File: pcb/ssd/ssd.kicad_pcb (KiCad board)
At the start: 2 copper layers, 68 parts, among them J101 GCT USB4105-GF-A, J301 NTC 接口 / XH 2.50mm, J302 BTL-004A / XH 2.50mm, Q201 BSS138, Q202 BSS138, SW101 启动（BOOT）, SW102 复位（RESET）, SW301 单位切换, U101 AP63203WU-7, U102 AP63205WU-7, U201 HT16K33 / SOP28, U301 SN74LVC1G17DCKR, U401 STM32C562CET6, Y401 24MHz / CL=10pF

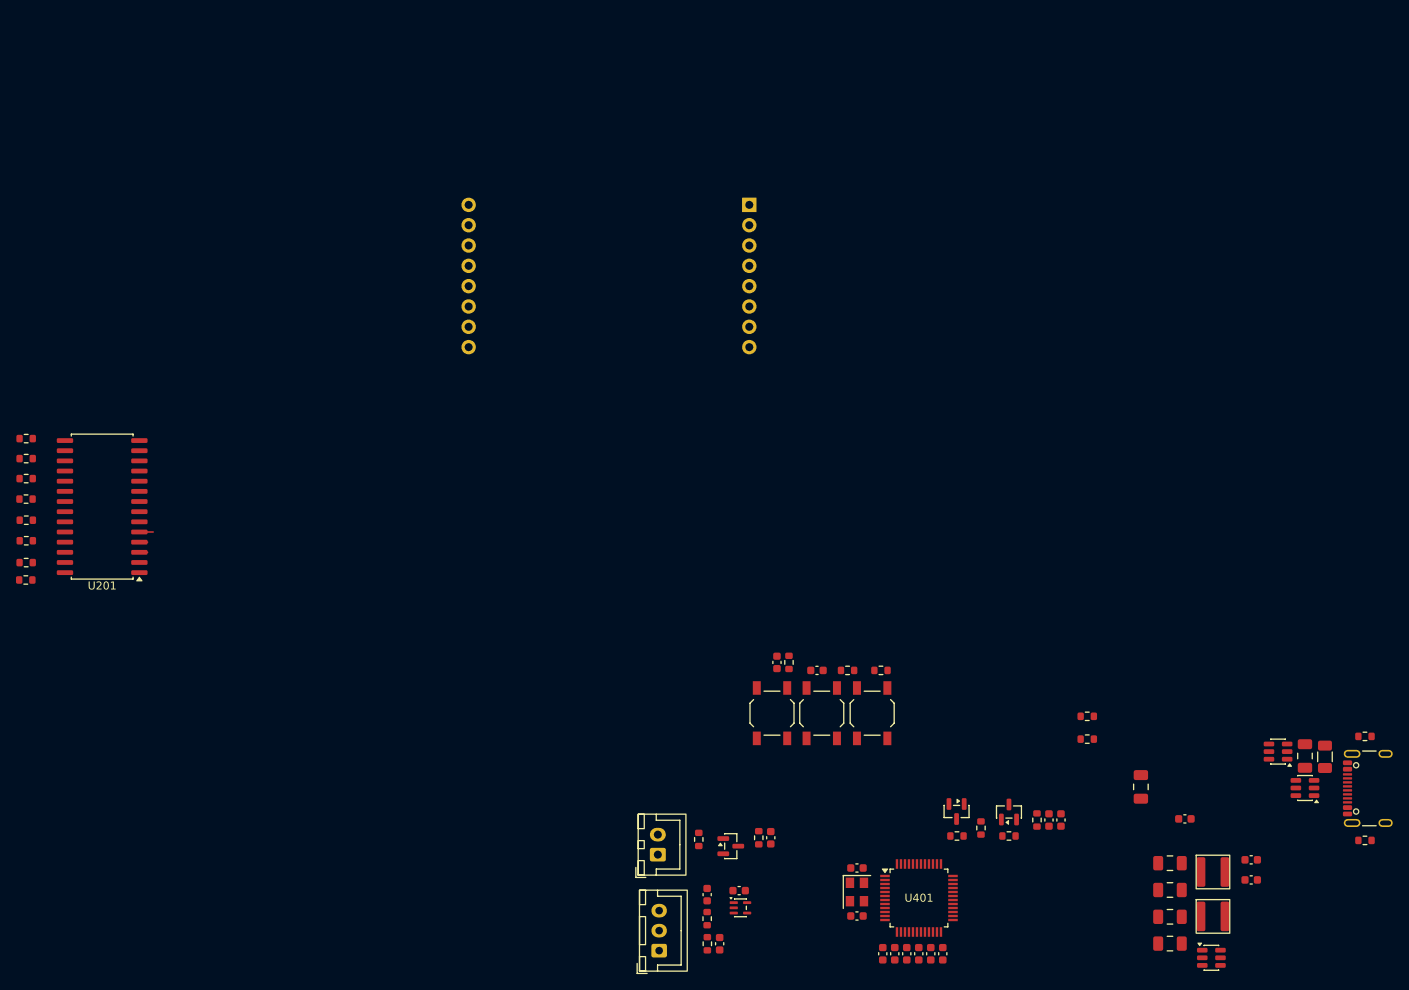
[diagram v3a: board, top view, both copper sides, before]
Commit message: 更新 Type-C 供电与 J-Link 调试设计
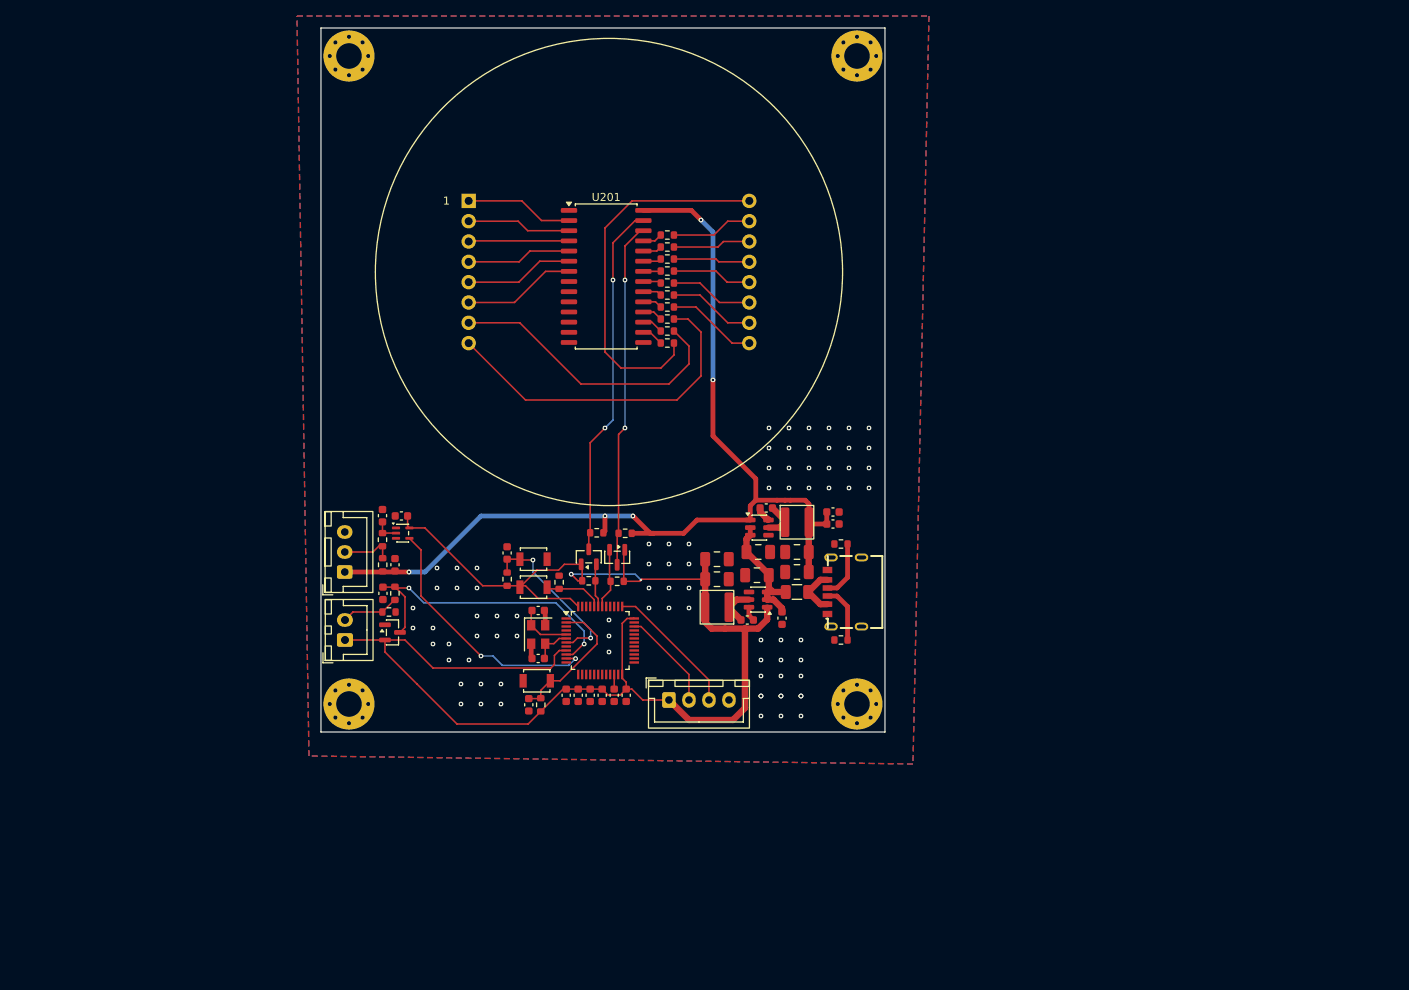
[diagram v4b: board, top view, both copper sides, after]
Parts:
- removed D101: USBLC6-2SC6, SSD:Package_TO_SOT_SMD__SOT-23-6
- added J102: SWD / XH 2.50mm, SSD:Connector_JST__JST_XH_B4B-XH-A_1x04_P2.50mm_Vertical, F.Cu at (150.0, 122.0)
- added REF**: MountingHole_3.2mm_M3_Pad_Via, MountingHole:MountingHole_3.2mm_M3_Pad_Via, F.Cu at (173.5, 122.5)
- added REF**: MountingHole_3.2mm_M3_Pad_Via, MountingHole:MountingHole_3.2mm_M3_Pad_Via, F.Cu at (110.0, 122.5)
- added REF**: MountingHole_3.2mm_M3_Pad_Via, MountingHole:MountingHole_3.2mm_M3_Pad_Via, F.Cu at (173.5, 41.5)
- added REF**: MountingHole_3.2mm_M3_Pad_Via, MountingHole:MountingHole_3.2mm_M3_Pad_Via, F.Cu at (110.0, 41.5)
- DS201: moved to F.Cu
- J101: value GCT USB4105-GF-A -> SHOU HAN TYPE-C 6P(073); footprint SSD:Connector_USB__USB_C_Receptacle_GCT_USB4105-xx-A_16P_TopMnt_Horizontal -> SSD:Connector_USB__SHOU_HAN_TYPE-C-6P-073_C668623
- SW101, SW102, SW301: footprint SSD:Button_Switch_SMD__SW_SPST_TL3342 -> SSD:Button_Switch_SMD__SW_SPST_B3U-1000P
- moved R207 87.2 mm to (149.8, 72.9), turned to 0 degrees
- moved R206 86.8 mm to (149.8, 71.4), turned to 0 degrees
- moved R205 86.4 mm to (149.8, 69.9), turned to 0 degrees
- moved R204 86.0 mm to (149.8, 68.4), turned to 0 degrees
- moved R203 85.6 mm to (149.8, 66.9), turned to 0 degrees
- moved R202 85.2 mm to (149.8, 65.4), turned to 0 degrees
- moved R201 84.9 mm to (149.8, 63.9), turned to 0 degrees
- moved R210 81.0 mm to (149.8, 77.4), turned to 0 degrees
- moved U102 78.0 mm to (161.3, 100.5)
- moved C109 76.4 mm to (162.2, 98.0)
- moved R209 73.2 mm to (149.8, 75.9)
- moved R208 72.3 mm to (149.8, 74.4), turned to 0 degrees
- moved C102 72.1 mm to (161.0, 106.4), turned to 180 degrees
- moved L102 71.6 mm to (166.0, 99.8)
- moved C110 71.0 mm to (161.2, 103.5)
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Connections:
- U401 pad 32: USB_DM -> unconnected-(U401-PA11-Pad32)
- U401 pad 33: USB_DP -> unconnected-(U401-PA12-Pad33)
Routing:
- net +3V3: track 0.00 -> 186.4 mm, vias 0 -> 2
- net +5V: track 0.00 -> 127.5 mm, vias 0 -> 5
- net Net-(DS201-J): track 0.00 -> 46.6 mm
- net Net-(Q202-D): track 0.00 -> 44.5 mm, vias 0 -> 2
- net Net-(Q201-D): track 0.00 -> 43.3 mm, vias 0 -> 2
- net Net-(DS201-H): track 0.00 -> 42.8 mm
- net NTC_ADC: track 0.00 -> 38.4 mm, vias 0 -> 2
- net Net-(DS201-I): track 0.00 -> 36.6 mm
- net FLOW_PULSE: track 0.00 -> 32.3 mm, vias 0 -> 2
- net MCU_NRST: track 0.00 -> 21.0 mm, vias 0 -> 2
- net USER_KEY: track 0.00 -> 17.5 mm
- net SWCLK: track 0.00 -> 17.2 mm
- net VIN_SYS: track 0.00 -> 15.7 mm
- net Net-(DS201-COM6): track 0.00 -> 14.2 mm
- net Net-(DS201-COM5): track 0.00 -> 13.6 mm
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- added copper zone on B.Cu, net GND
- added copper zone on F.Cu, net GND
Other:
- board outline added: 70.5 x 88 mm

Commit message: 添加缝合孔
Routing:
- net GND: vias 82 -> 485

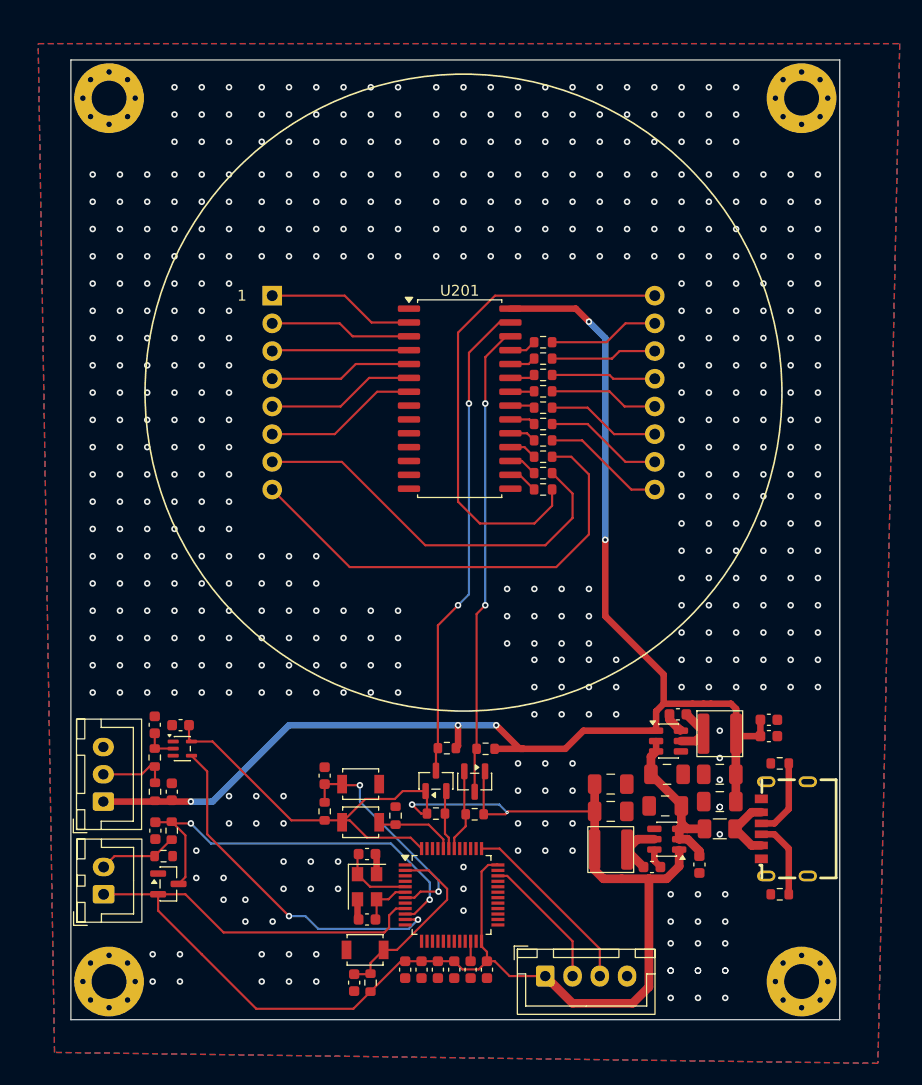
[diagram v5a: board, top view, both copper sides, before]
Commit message: 更新 PCB 布局与项目文档
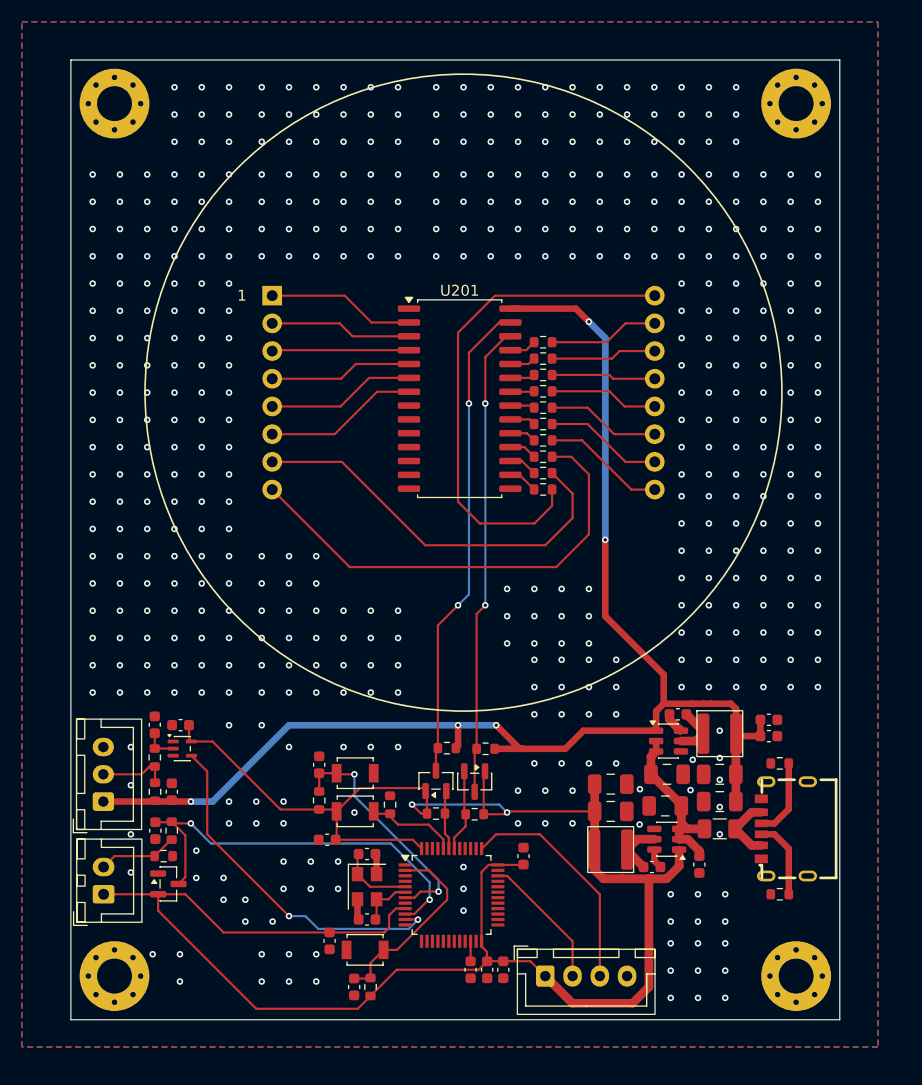
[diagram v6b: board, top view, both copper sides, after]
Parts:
- moved C401 16.7 mm to (130.0, 109.5), turned to 180 degrees
- moved C406 14.7 mm to (130.2, 118.8)
- moved C402 13.0 mm to (148.0, 111.0), turned to 90 degrees
- moved C404 9.00 mm to (146.1, 121.4)
- moved C403 6.02 mm to (144.7, 121.4)
- moved C104 1.12 mm to (129.3, 102.6)
- moved R103 1.12 mm to (135.8, 106.3)
- moved R104 1.12 mm to (129.3, 105.9)
- moved SW101 1.12 mm to (132.6, 106.9)
- moved SW102 1.12 mm to (132.6, 103.4)
- moved REF** 0.71 mm to (173.0, 122.0)
- moved REF** 0.71 mm to (110.5, 122.0)
- moved REF** 0.71 mm to (173.0, 42.0)
- moved REF** 0.71 mm to (110.5, 42.0)
- moved C305 0.40 mm to (132.5, 123.0)
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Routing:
- net SWCLK: track 17.2 -> 21.2 mm
- net +3V3: track 186.4 -> 189.9 mm
- net MCU_NRST: track 21.0 -> 22.2 mm
- net MCU_BOOT0: track 7.38 -> 8.46 mm
- net GND: vias 485 -> 493
